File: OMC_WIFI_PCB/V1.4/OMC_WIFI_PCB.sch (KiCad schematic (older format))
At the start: 23 parts, among them J1 Conn_01x02_Male, J2 Conn_01x02_Female, J3 Conn_01x02_Male, J4 Switch, J5 Pins_FT232R, J6 Level shifter, J8 Regulador, K1 SLA-12VDC-SL-C, Q1 2N3904, U1 ESP32-WROOM-32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

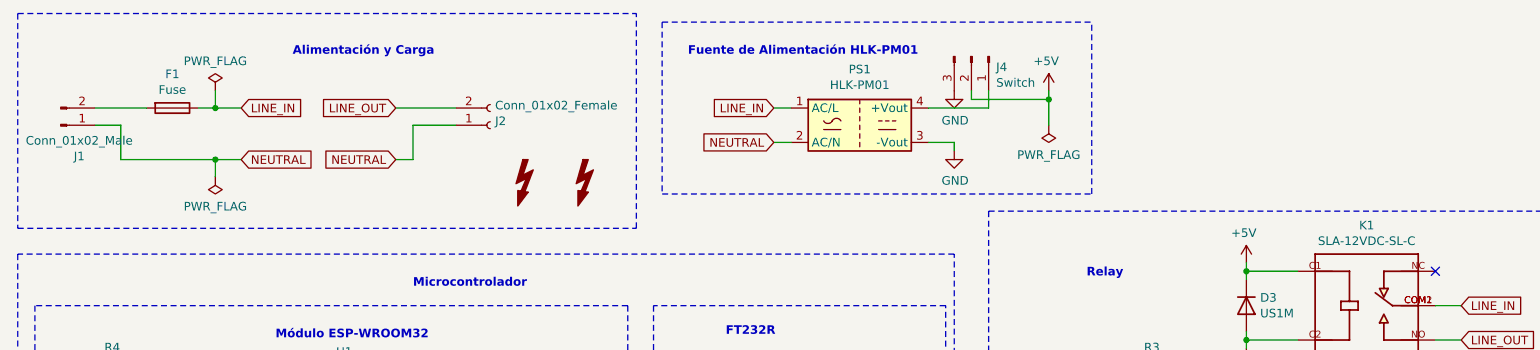
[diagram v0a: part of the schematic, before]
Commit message: Creación de versión 1.4 PCB
> Cambio en diseño para paso de cable por toroide.
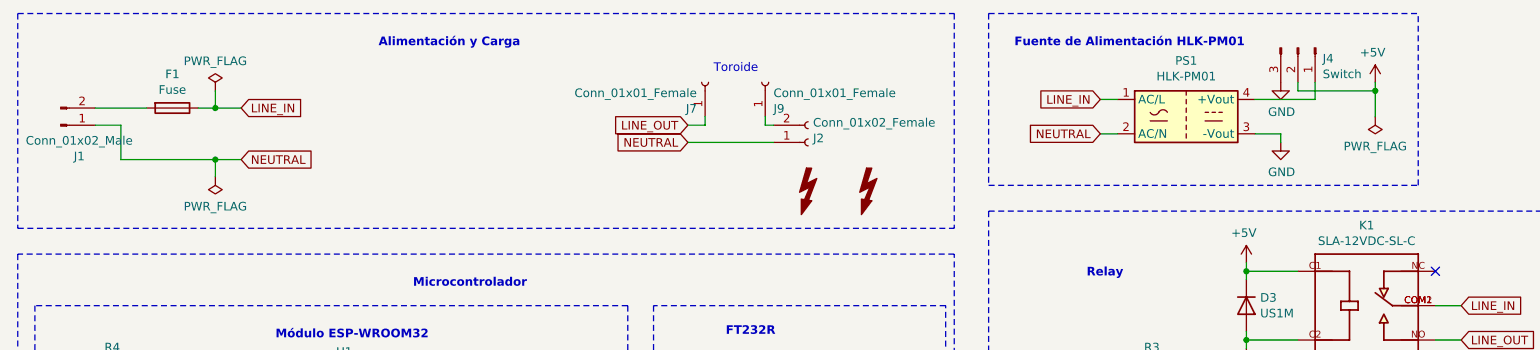
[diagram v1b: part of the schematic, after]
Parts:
- added J7, J9: Conn_01x01_Female, Connector_Pin:Pin_D1.3mm_L10.0mm_W3.5mm_Flat, symbol Connector:Conn_01x01_Female
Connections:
- net LINE_OUT: now also J7.1 (Pin_1); no longer J2.2 (Pin_2)
- new net: J2.2 (Pin_2), J9.1 (Pin_1)
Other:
- note added: "Toroide"
- moved on the sheet: J2, J4, PS1

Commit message: Primer código pruebas PZEM
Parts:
- added J10: Conn_01x01_Male, Connector_PinHeader_2.54mm:PinHeader_1x01_P2.54mm_Vertical, symbol Connector:Conn_01x01_Male
- J4: footprint Connector_Wire:SolderWire-0.75sqmm_1x03_P4.8mm_D1.25mm_OD2.3mm -> Connector_PinHeader_2.54mm:PinHeader_1x03_P2.54mm_Vertical
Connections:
- net GND: now also J4.1 (Pin_1); no longer J4.3 (Pin_3)
- net at PS1.4 (+Vout): now also J4.3 (Pin_3); no longer J4.1 (Pin_1)
- net TOUCH: now reaches U1.8 (IO32)
- net TOUCH: now also J10.1 (Pin_1)
- no-connect marks 30 -> 29
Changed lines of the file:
@@
 F 0 "J4" V 8262 944 50  0000 L CNN
 F 1 "Switch" V 8353 944 50  0000 L CNN
-F 2 "Connector_Wire:SolderWire-0.75sqmm_1x03_P4.8mm_D1.25mm_OD2.3mm" H 8200 800 50  0001 C CNN
+F 2 "Connector_PinHeader_2.54mm:PinHeader_1x03_P2.54mm_Vertical" H 8200 800 50  0001 C CNN
 F 3 "~" H 8200 800 50  0001 C CNN
 	1    8200 800
-	0    1    1    0
+	0    -1   1    0
 $EndComp
 Wire Wire Line
@@
 Wire Wire Line
 	3250 4350 3450 4350
-NoConn ~ 3450 4950
 Wire Wire Line
 	3250 4450 3450 4450
@@
 Wire Wire Line
 	4650 1350 5150 1350
+Text GLabel 3450 4950 2    50   Input ~ 0
+TOUCH
+Text GLabel 9500 1000 0    50   Input ~ 0
+TOUCH
+$Comp
+L Connector:Conn_01x01_Male J10
+U 1 1 627E9A98
+P 9700 1000
+F 0 "J10" H 9672 932 50  0000 R CNN
+F 1 "Conn_01x01_Male" H 9672 1023 50  0000 R CNN
+F 2 "Connector_PinHeader_2.54mm:PinHeader_1x01_P2.54mm_Vertical" H 9700 1000 50  0001 C CNN
+F 3 "~" H 9700 1000 50  0001 C CNN
+	1    9700 1000
+	-1   0    0    1
+$EndComp
 $EndSCHEMATC

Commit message: Creación de nuevas librerías conectores AC
Creación de librería 2D para conectores macho y hembra para AC
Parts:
- J1: footprint omc-plugs:OMC-Male-Plug -> NEMA_5_P:NEMA_5_P; symbol Connector:Conn_01x02_Male -> Connector:Conn_01x03_Male
- J2: footprint omc-schematics LE:OMC-Female-Plug -> NEMA_5_R:NEMA_5_R; symbol Connector:Conn_01x02_Female -> Connector:Conn_01x03_Female
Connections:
- net NEUTRAL: now also J1.2 (Pin_2), J2.2 (Pin_2); no longer J1.1 (Pin_1), J2.1 (Pin_1)
- net at F1.2: now also J1.1 (Pin_1); no longer J1.2 (Pin_2)
- net at J9.1 (Pin_1): now also J2.1 (Pin_1); no longer J2.2 (Pin_2)
- new net AC_GROUND: J1.3 (Pin_3), J2.3 (Pin_3)
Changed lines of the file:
@@
 	750  600  750  1850
 $Comp
-L Connector:Conn_01x02_Male J1
+L Connector:Conn_01x03_Male J1
 U 1 1 62564E0F
 P 1000 1250
 F 0 "J1" H 1108 1431 50  0000 C CNN
 F 1 "Conn_01x02_Male" H 1108 1340 50  0000 C CNN
-F 2 "omc-plugs:OMC-Male-Plug" H 1000 1250 50  0001 C CNN
+F 2 "NEMA_5_P:NEMA_5_P" H 1000 1250 50  0001 C CNN
 F 3 "~" H 1000 1250 50  0001 C CNN
 	1    1000 1250
-	1    0    0    1
+	1    0    0    -1
 $EndComp
 Wire Wire Line
@@
 	3250 4450 3450 4450
 $Comp
-L Connector:Conn_01x02_Female J2
+L Connector:Conn_01x03_Female J2
 U 1 1 626943A8
 P 5350 1350
 F 0 "J2" H 5378 1326 50  0000 L CNN
 F 1 "Conn_01x02_Female" H 5378 1235 50  0000 L CNN
-F 2 "omc-schematics LE:OMC-Female-Plug" H 5350 1350 50  0001 C CNN
+F 2 "NEMA_5_R:NEMA_5_R" H 5350 1350 50  0001 C CNN
 F 3 "~" H 5350 1350 50  0001 C CNN
 	1    5350 1350
-	1    0    0    1
+	1    0    0    -1
 $EndComp
 $Comp
@@
 	-1   0    0    1
 $EndComp
+Text GLabel 1250 1600 2    50   Input ~ 0
+AC_GROUND
+Wire Wire Line
+	1200 1350 1200 1600
+Wire Wire Line
+	1200 1600 1250 1600
+Text GLabel 5150 1450 0    50   Input ~ 0
+AC_GROUND
 $EndSCHEMATC
